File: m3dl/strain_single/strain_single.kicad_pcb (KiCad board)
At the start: 2 copper layers, 40 x 33 mm, 66 parts, among them IC1 AD8226, IC2 AD8541, IC3 AD8226, IC4 AD8541, IC5 AD8656, IC6 AD8226, IC7 AD8541, IC8 AD8656, IC9 AD8656, J1 WEST TOP, J2 EAST TOP, J3 WEST BOT, J4 EAST BOT, J5 NORTH TOP, J6 NORTH BOT, J7 S1, J8 S3, J9 S2

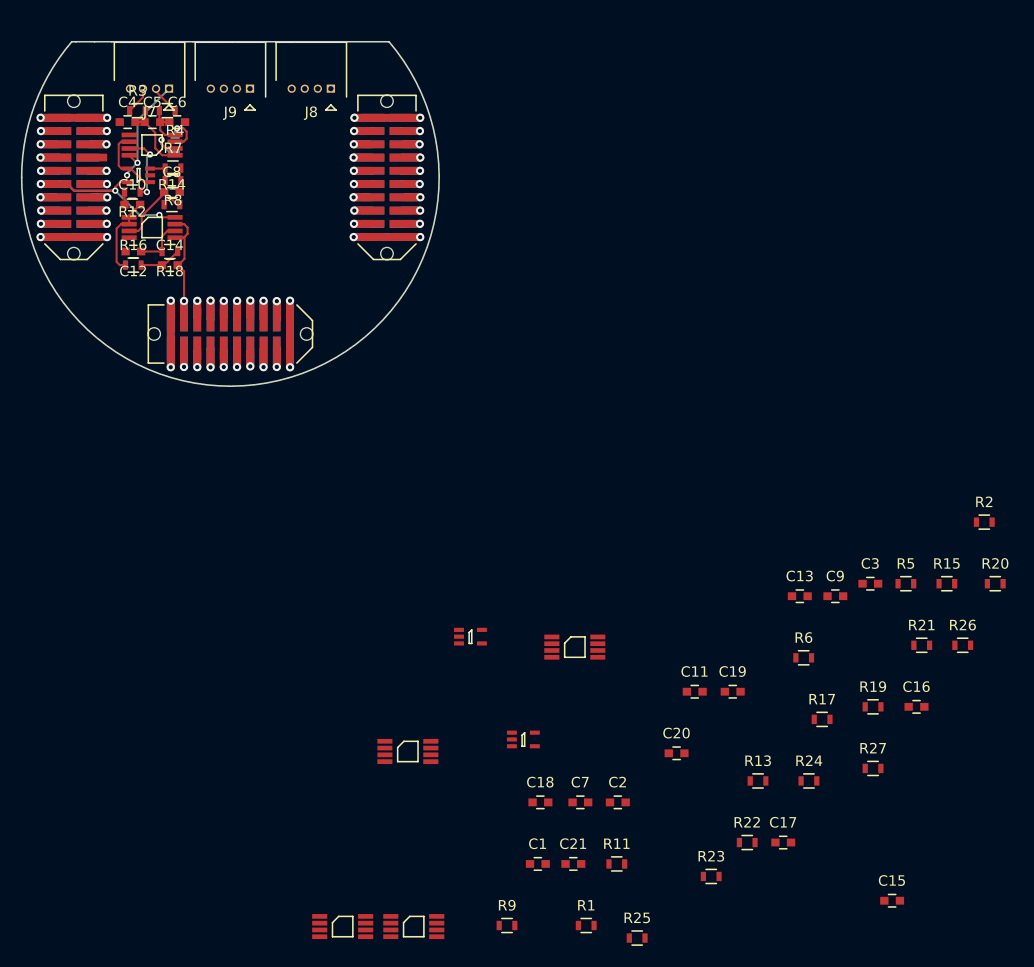
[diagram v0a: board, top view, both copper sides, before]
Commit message: Placed all components on Strain Board
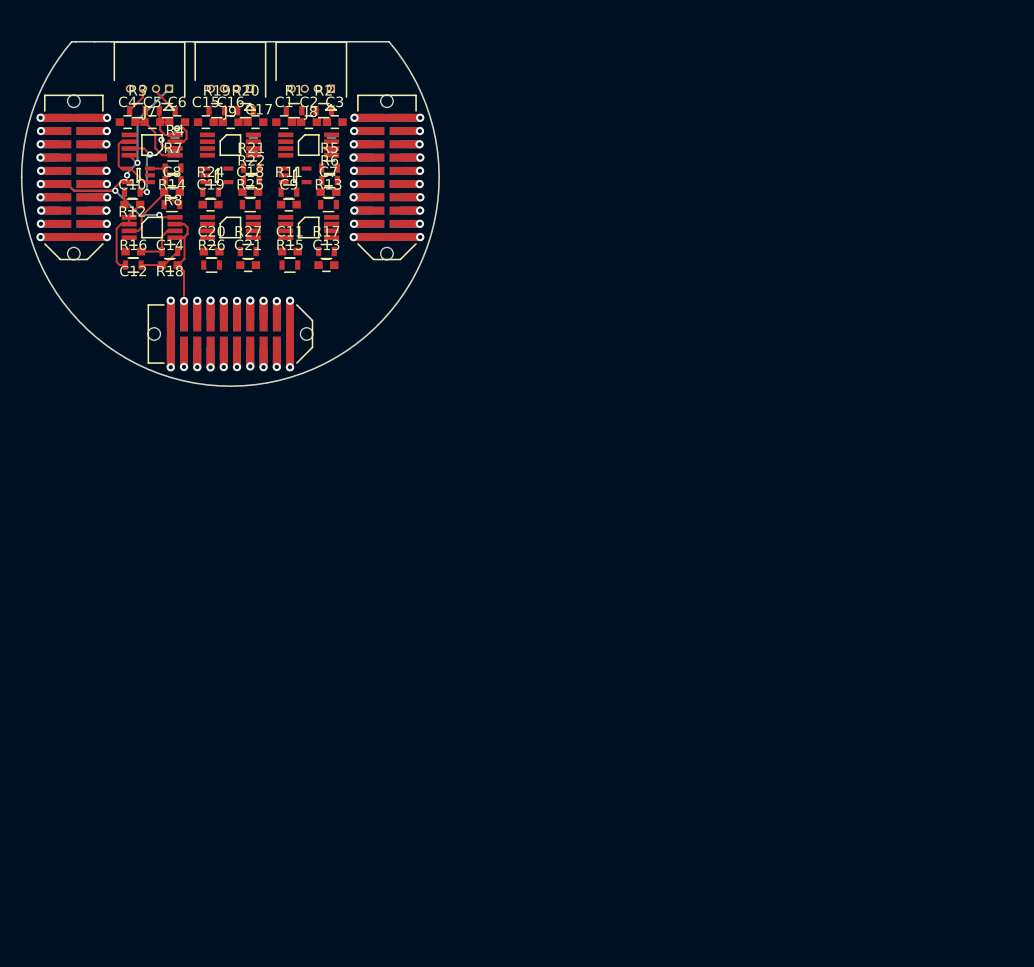
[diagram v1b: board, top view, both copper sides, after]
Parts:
- R23, R9: moved to B.Cu
- moved C15 99.4 mm to (97.7, 94.7)
- moved C16 86.4 mm to (100.0, 94.7)
- moved C17 85.6 mm to (102.4, 94.7)
- moved R19 84.9 mm to (98.7, 93.6)
- moved R20 84.9 mm to (101.5, 93.6)
- moved R1 82.9 mm to (106.1, 93.6)
- moved R23 82.8 mm to (102.2, 96.8), turned to 90 degrees
- moved R26 80.7 mm to (98.2, 108.4)
- moved R24 80.4 mm to (98.1, 101.4)
- moved R25 79.5 mm to (101.9, 102.6)
- moved R22 79.3 mm to (102.0, 100.3)
- moved R21 78.8 mm to (102.0, 99.1)
- moved R27 77.7 mm to (101.7, 107.1)
- moved IC6 76.9 mm to (100.0, 96.9)
- moved R9 76.7 mm to (109.7, 96.8), turned to 90 degrees
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
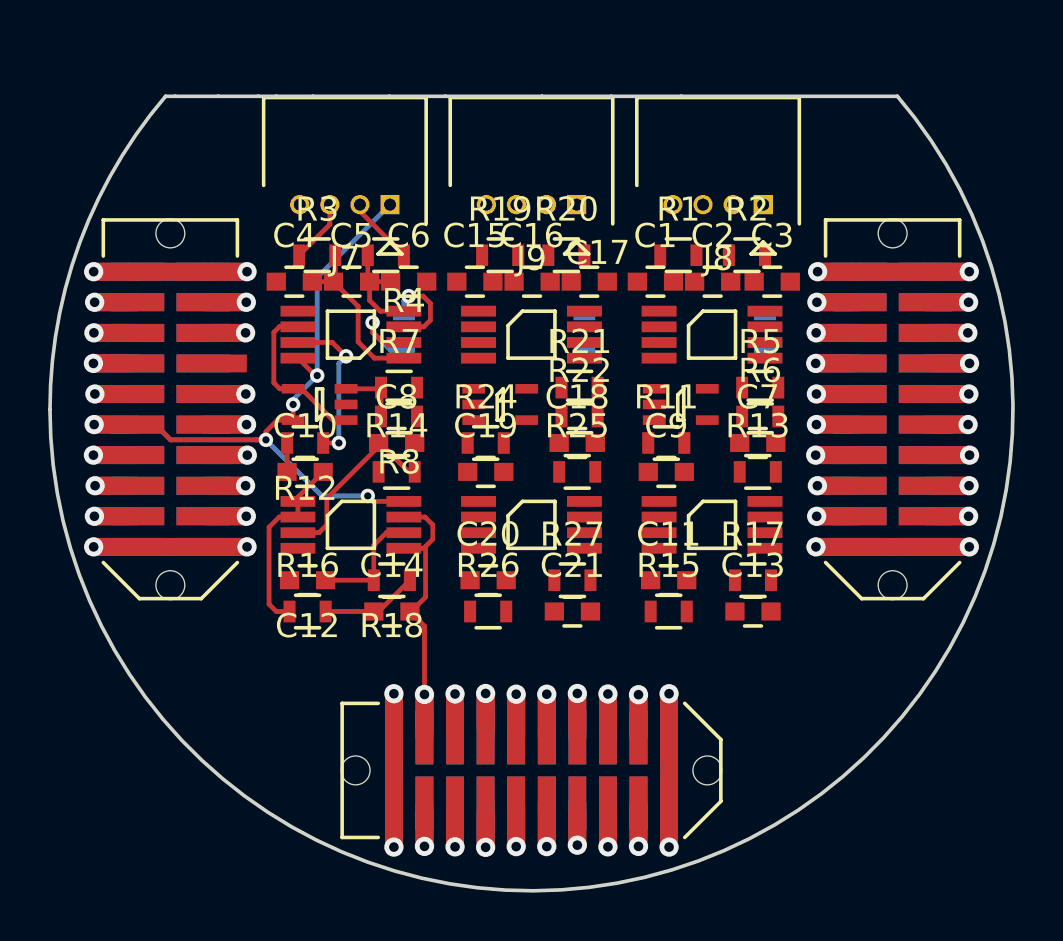
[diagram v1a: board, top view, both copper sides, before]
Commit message: Finished routing Strain Gauge PCB - Needs Silkscreen
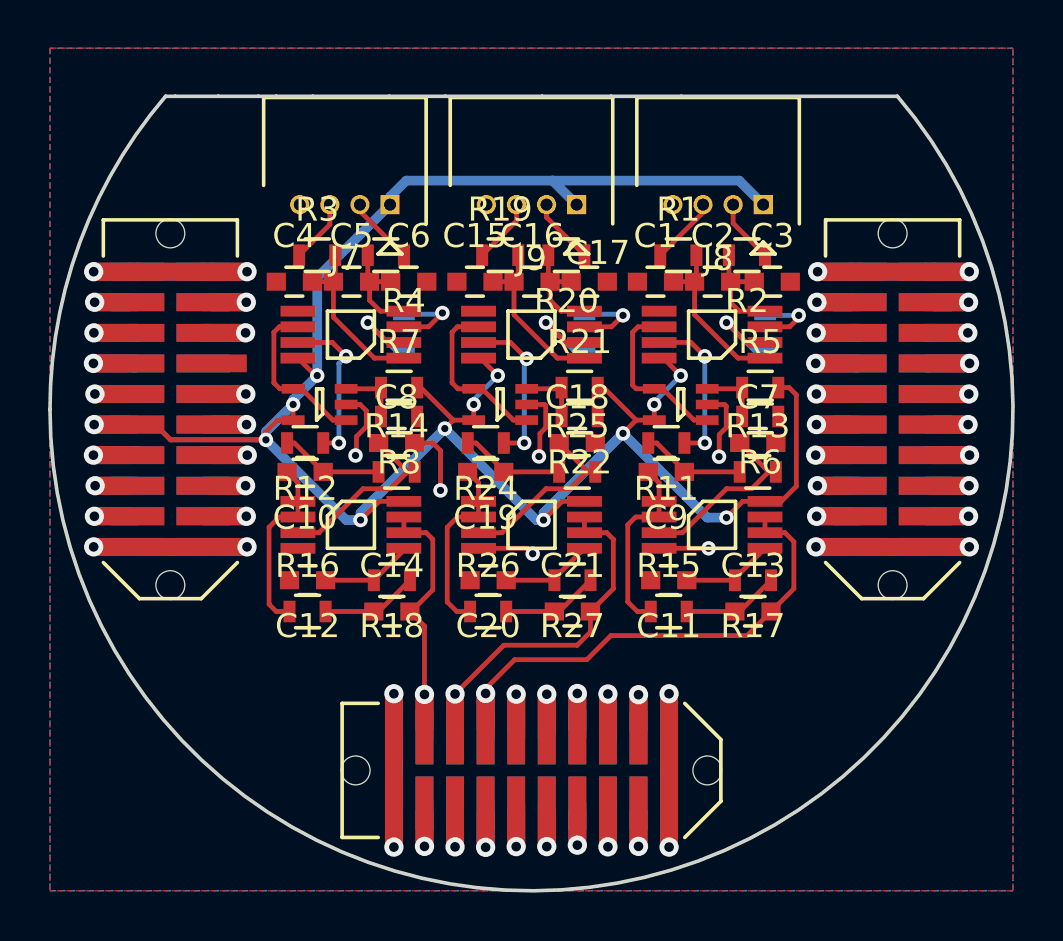
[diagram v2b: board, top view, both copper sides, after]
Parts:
- turned C10 to 180 degrees
- turned C11 to 180 degrees
- turned C19 to 180 degrees
- turned C20 to 180 degrees
- turned C9 to 180 degrees
- turned IC1 to 180 degrees
- turned IC2 to 180 degrees
- turned IC6 to 180 degrees
- turned IC7 to 180 degrees
- turned R11 to 180 degrees
- turned R17 to 180 degrees
- turned R2 to 180 degrees
- turned R20 to 180 degrees
- turned R22 to 180 degrees
- turned R23 to 270 degrees
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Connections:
- IC5 pad 5: /STRAIN1 -> Net-(C12-Pad1)
- IC5 pad 6: Net-(C12-Pad1) -> /STRAIN1
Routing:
- net 3v3: track 35.0 -> 101.2 mm, vias 5 -> 13
- net /STRAIN3: track 3.31 -> 22.0 mm
- net GND: track 76.3 -> 92.6 mm, vias 12 -> 18
- net /STRAIN2: track 3.27 -> 16.2 mm
- net Net-(C9-Pad2): track 0.00 -> 7.81 mm
- net Net-(C19-Pad2): track 0.00 -> 7.75 mm
- net Net-(C7-Pad1): track 0.00 -> 7.59 mm
- net Net-(C18-Pad1): track 0.00 -> 7.57 mm
- net Net-(IC1-Pad6): track 0.00 -> 7.09 mm
- net Net-(C15-Pad2): track 0.00 -> 7.09 mm
- net Net-(C1-Pad2): track 0.00 -> 7.05 mm
- net Net-(IC6-Pad6): track 0.00 -> 7.04 mm
- net Net-(IC6-Pad7): track 0.00 -> 6.67 mm, vias 0 -> 2
- net Net-(IC1-Pad7): track 0.00 -> 6.59 mm, vias 0 -> 2
- net Net-(C2-Pad2): track 0.00 -> 4.55 mm
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- added copper zone on B.Cu, net GND
- added copper zone on F.Cu, net GND

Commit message: Finished routing Pressure PCB - Needs Silkscreen
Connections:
- J1 pad 8: /JTDO -> /JTDI
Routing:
- net /JTDI: track 0.00 -> 3.31 mm, vias 0 -> 1

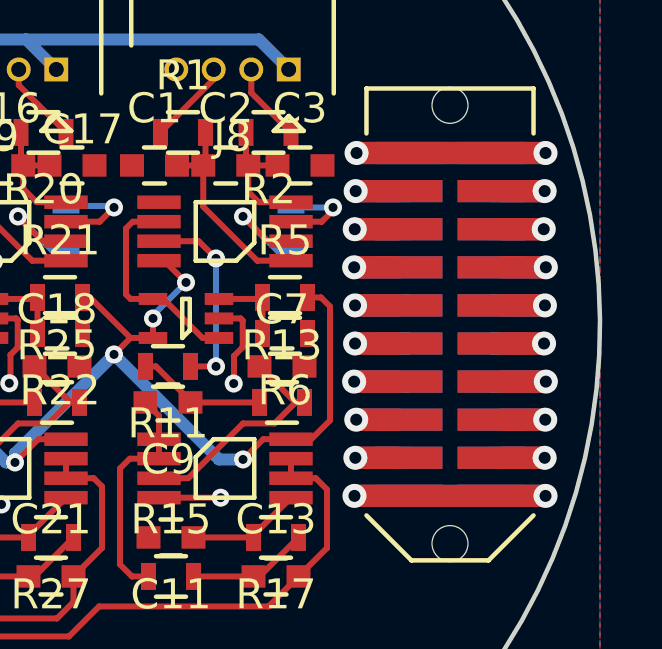
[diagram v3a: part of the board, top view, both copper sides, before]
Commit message: Tidyied up Main & Checked Connector Clearance for Sensors
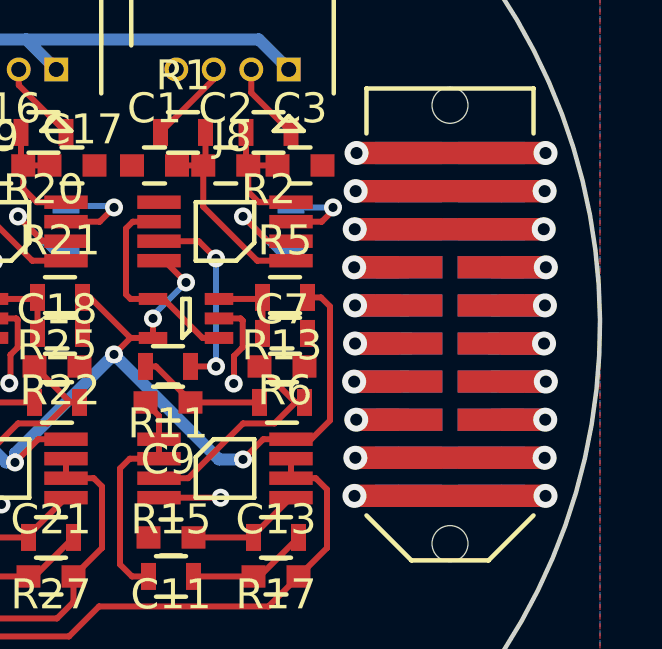
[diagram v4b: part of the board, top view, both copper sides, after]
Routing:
- net /PYRO_SO: track 6.44 -> 12.6 mm
- net /PYRO_SI: track 6.44 -> 12.6 mm
- net /CHARGE: track 6.46 -> 12.6 mm
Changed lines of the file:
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@@
     (links 203)
     (no_connects 3)
-    (area 79.923999 86.924999 120.076001 120.076001)
+    (area 79.85 79.899999 120.100001 120.100001)
     (thickness 1.6)
     (drawings 24)
-    (tracks 537)
+    (tracks 543)
     (zones 0)
     (modules 66)
@@
   (via (at 88.155 104.445) (size 0.8) (drill 0.4) (layers F.Cu B.Cu) (net 55))
   (segment (start 86.715 104.445) (end 88.155 104.445) (width 0.74) (layer F.Cu) (net 55))
+  (segment (start 113.635 95.555) (end 116.365 95.555) (width 0.74) (layer B.Cu) (net 56))
+  (segment (start 116.715 95.555) (end 113.285 95.555) (width 0.74) (layer F.Cu) (net 56))
   (segment (start 113.635 95.555) (end 111.855 95.555) (width 0.74) (layer B.Cu) (net 56))
   (segment (start 118.155 95.555) (end 116.365 95.555) (width 0.74) (layer B.Cu) (net 56))
@@
   (via (at 111.855 95.555) (size 0.8) (drill 0.4) (layers F.Cu B.Cu) (net 56))
   (segment (start 113.285 95.555) (end 111.855 95.555) (width 0.74) (layer F.Cu) (net 56))
+  (segment (start 113.635 96.825) (end 116.365 96.825) (width 0.74) (layer B.Cu) (net 57))
+  (segment (start 113.285 96.825) (end 116.715 96.825) (width 0.74) (layer F.Cu) (net 57))
   (segment (start 111.825 96.825) (end 113.635 96.825) (width 0.74) (layer B.Cu) (net 57))
   (segment (start 118.125 96.825) (end 116.365 96.825) (width 0.74) (layer B.Cu) (net 57))
@@
   (via (at 118.175 103.175) (size 0.8) (drill 0.4) (layers F.Cu B.Cu) (net 67))
   (segment (start 116.715 103.175) (end 118.175 103.175) (width 0.74) (layer F.Cu) (net 67))
+  (segment (start 113.635 104.445) (end 116.365 104.445) (width 0.74) (layer B.Cu) (net 68))
+  (segment (start 116.715 104.445) (end 113.285 104.445) (width 0.74) (layer F.Cu) (net 68))
   (segment (start 116.365 104.445) (end 118.155 104.445) (width 0.74) (layer B.Cu) (net 68))
   (segment (start 111.845 104.445) (end 113.635 104.445) (width 0.74) (layer B.Cu) (net 68))

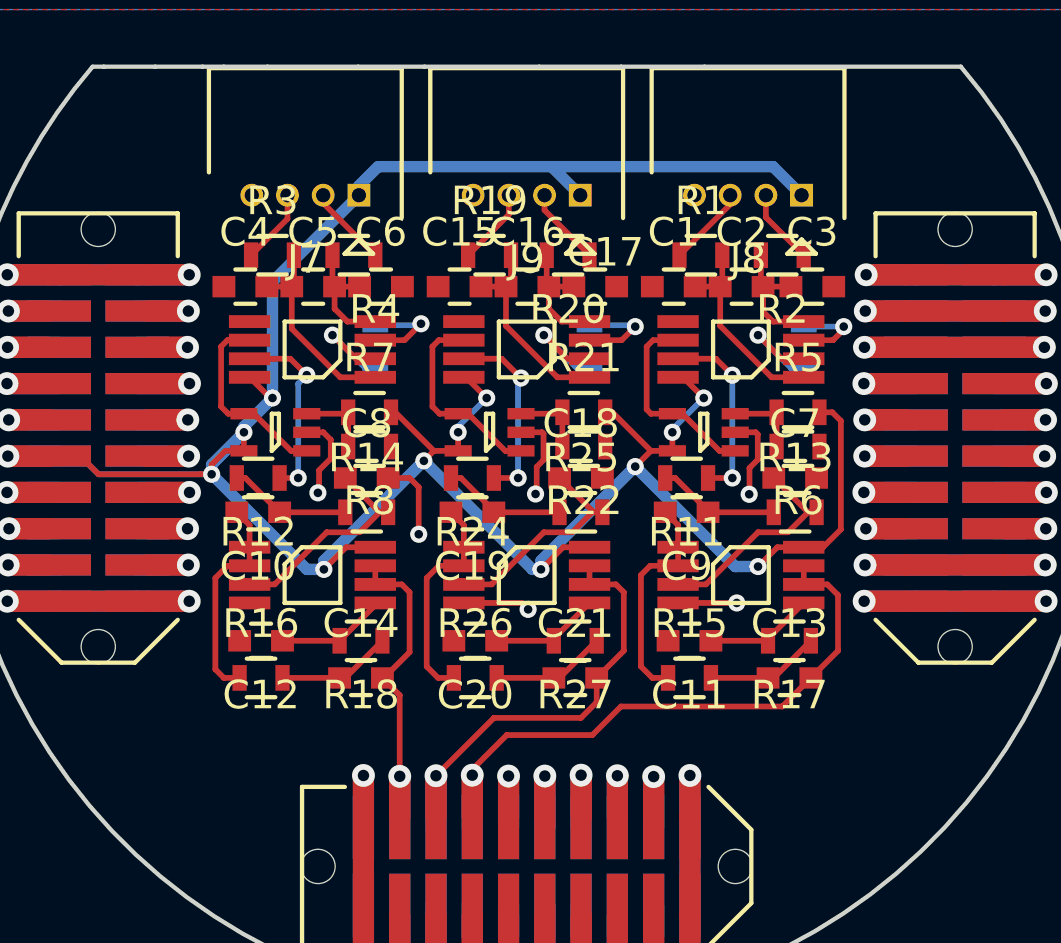
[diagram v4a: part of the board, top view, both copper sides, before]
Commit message: Completed all of Pressure Strain and Temperature
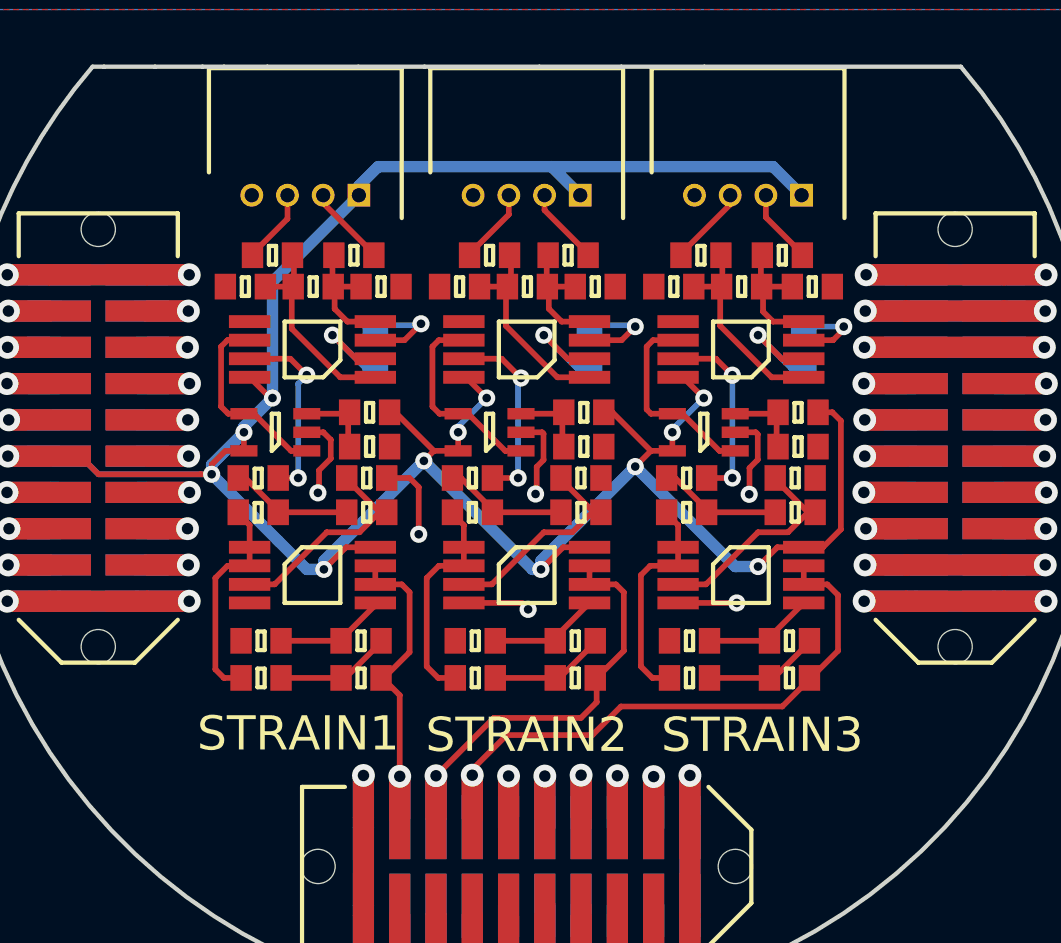
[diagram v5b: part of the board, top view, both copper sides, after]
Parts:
- C1, C10, C11, C12, C13, C14, C15, C16, C17, C18, C19, C2, C20, C21, C3, C4, C5, C6, C7, C8, C9: footprint Capacitors_SMD:C_0603 -> agg:0603-L
- R1, R10, R11, R12, R13, R14, R15, R16, R17, R18, R19, R2, R20, R21, R22, R23, R24, R25, R26, R27, R3, R4, R5, R6, R7, R8, R9: footprint Resistors_SMD:R_0603 -> agg:0603-L
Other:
- board text added: "3V3"
- board text added: "GND"
- board text added: "R10"
- board text added: "R23"
- board text added: "R9"
- board text added: "SG1+"
- board text added: "SG1-"
- board text added: "SG2+"
- board text added: "SG2-"
- board text added: "SG3+"
- board text added: "SG3-"
- board text added: "STRAIN1"
- board text added: "STRAIN2"
- board text added: "STRAIN3"
